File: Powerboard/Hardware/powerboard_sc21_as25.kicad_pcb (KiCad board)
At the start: 4 copper layers, 86.3 x 55.6 mm, 151 parts, among them IC1 BQ24618RGET-iclr, IC2 CP2102, J1 Thermistor Connection 103AT N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, J10 Conn_01x04_Male, J11 Conn_01x03_MountingPin, J2 Conn_01x02_Male, J3 Conn_01x02_Male, J4 Conn_01x08_Male, J5 Conn_01x04_Male, J6 Conn_01x02_Male, J7 IsolationSwitch, J8 USB_C_Receptacle_USB2.0, J9 Conn_Coaxial, Q1 RSJ250P10TL, Q10 MCH6351, Q2 RSJ250P10TL, Q3 RSJ250P10TL, Q4 RS1G120MN, Q5 RS1G120MN, Q6 MMDT2222A, Q7 RSJ250P10TL, Q8 RSJ250P10TL, Q9 MCH6351, U1 LTC4412xS6, U11 LTC4411, U2 SN65HVD230, U3 ESP32-PICO-D4, U4 SC4216H, U6 LM2679T-3.3-iclr, U7 LM2679T-3.3-iclr, U8 LTC4412xS6, U9 LTC4412xS6

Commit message: made can h and can l lines closer in length
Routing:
- net /CANL: track 38.5 -> 37.1 mm
- net GND: vias 298 -> 297
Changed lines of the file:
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@@
   (via (at 134.5 52.5) (size 0.8) (drill 0.4) (layers "F.Cu" "B.Cu") (free) (net 2))
   (via (at 126.4 63.197) (size 0.8) (drill 0.4) (layers "F.Cu" "B.Cu") (free) (net 2))
-  (via (at 95.8155 71.3) (size 0.8) (drill 0.4) (layers "F.Cu" "B.Cu") (free) (net 2))
   (via (at 117.5 78) (size 0.8) (drill 0.4) (layers "F.Cu" "B.Cu") (free) (net 2))
   (via (at 103 36.5) (size 0.8) (drill 0.4) (layers "F.Cu" "B.Cu") (free) (net 2))
@@
   (segment (start 75.745155 57.598081) (end 75.158096 57.011022) (width 0.25) (layer "B.Cu") (net 37))
   (segment (start 75.158096 57.011022) (end 75.158096 56.410831) (width 0.25) (layer "B.Cu") (net 37))
-  (segment (start 96.98952 71.84352) (end 96.98952 70.635866) (width 0.25) (layer "B.Cu") (net 39))
+  (segment (start 96.54 80.16) (end 96.54 77.958) (width 0.25) (layer "B.Cu") (net 39))
+  (segment (start 101.300449 59.749551) (end 103.355449 61.804551) (width 0.25) (layer "B.Cu") (net 39))
   (segment (start 96.54 77.958) (end 98.552 75.946) (width 0.25) (layer "B.Cu") (net 39))
-  (segment (start 98.552 75.946) (end 98.552 73.406) (width 0.25) (layer "B.Cu") (net 39))
-  (segment (start 103.29799 66.316292) (end 104.736292 66.316292) (width 0.25) (layer "B.Cu") (net 39))
-  (segment (start 96.98952 70.635866) (end 97.575386 70.05) (width 0.25) (layer "B.Cu") (net 39))
-  (segment (start 101.300449 59.749551) (end 103.355449 61.804551) (width 0.25) (layer "B.Cu") (net 39))
-  (segment (start 96.54 80.16) (end 96.54 77.958) (width 0.25) (layer "B.Cu") (net 39))
+  (segment (start 98.552 73.406) (end 96.98952 71.84352) (width 0.25) (layer "B.Cu") (net 39))
   (segment (start 104.307949 61.804551) (end 104.307949 60.062051) (width 0.25) (layer "B.Cu") (net 39))
   (segment (start 103.355449 61.804551) (end 104.307949 61.804551) (width 0.25) (layer "B.Cu") (net 39))
-  (segment (start 98.552 73.406) (end 96.98952 71.84352) (width 0.25) (layer "B.Cu") (net 39))
+  (segment (start 105.02725 61.804551) (end 104.307949 61.804551) (width 0.25) (layer "B.Cu") (net 39))
+  (segment (start 99.564282 70.05) (end 103.29799 66.316292) (width 0.25) (layer "B.Cu") (net 39))
+  (segment (start 97.575386 70.05) (end 99.564282 70.05) (width 0.25) (layer "B.Cu") (net 39))
   (segment (start 101.300449 59.749551) (end 100.710449 59.749551) (width 0.25) (layer "B.Cu") (net 39))
-  (segment (start 99.564282 70.05) (end 103.29799 66.316292) (width 0.25) (layer "B.Cu") (net 39))
   (segment (start 98.385449 60.539551) (end 99.225449 59.699551) (width 0.25) (layer "B.Cu") (net 39))
+  (segment (start 96.98952 71.84352) (end 96.98952 70.635866) (width 0.25) (layer "B.Cu") (net 39))
   (segment (start 97.431521 62.259551) (end 98.385449 61.305623) (width 0.25) (layer "B.Cu") (net 39))
-  (segment (start 105.42 61.139102) (end 104.325449 60.044551) (width 0.25) (layer "B.Cu") (net 39))
+  (segment (start 105.41 65.642584) (end 105.41 62.187301) (width 0.25) (layer "B.Cu") (net 39))
+  (segment (start 96.98952 70.635866) (end 97.575386 70.05) (width 0.25) (layer "B.Cu") (net 39))
   (segment (start 99.225449 59.699551) (end 100.660449 59.699551) (width 0.25) (layer "B.Cu") (net 39))
   (segment (start 98.385449 61.305623) (end 98.385449 60.539551) (width 0.25) (layer "B.Cu") (net 39))
-  (segment (start 97.575386 70.05) (end 99.564282 70.05) (width 0.25) (layer "B.Cu") (net 39))
-  (segment (start 105.42 65.632584) (end 105.42 61.139102) (width 0.25) (layer "B.Cu") (net 39))
-  (segment (start 104.736292 66.316292) (end 105.42 65.632584) (width 0.25) (layer "B.Cu") (net 39))
+  (segment (start 98.552 75.946) (end 98.552 73.406) (width 0.25) (layer "B.Cu") (net 39))
+  (segment (start 105.41 62.187301) (end 105.02725 61.804551) (width 0.25) (layer "B.Cu") (net 39))
+  (segment (start 103.29799 66.316292) (end 104.736292 66.316292) (width 0.25) (layer "B.Cu") (net 39))
+  (segment (start 104.736292 66.316292) (end 105.41 65.642584) (width 0.25) (layer "B.Cu") (net 39))
   (segment (start 97.389188 69.60048) (end 96.54 70.449668) (width 0.25) (layer "B.Cu") (net 40))
   (segment (start 98.354969 64.9148) (end 99.219995 65.779826) (width 0.25) (layer "B.Cu") (net 40))

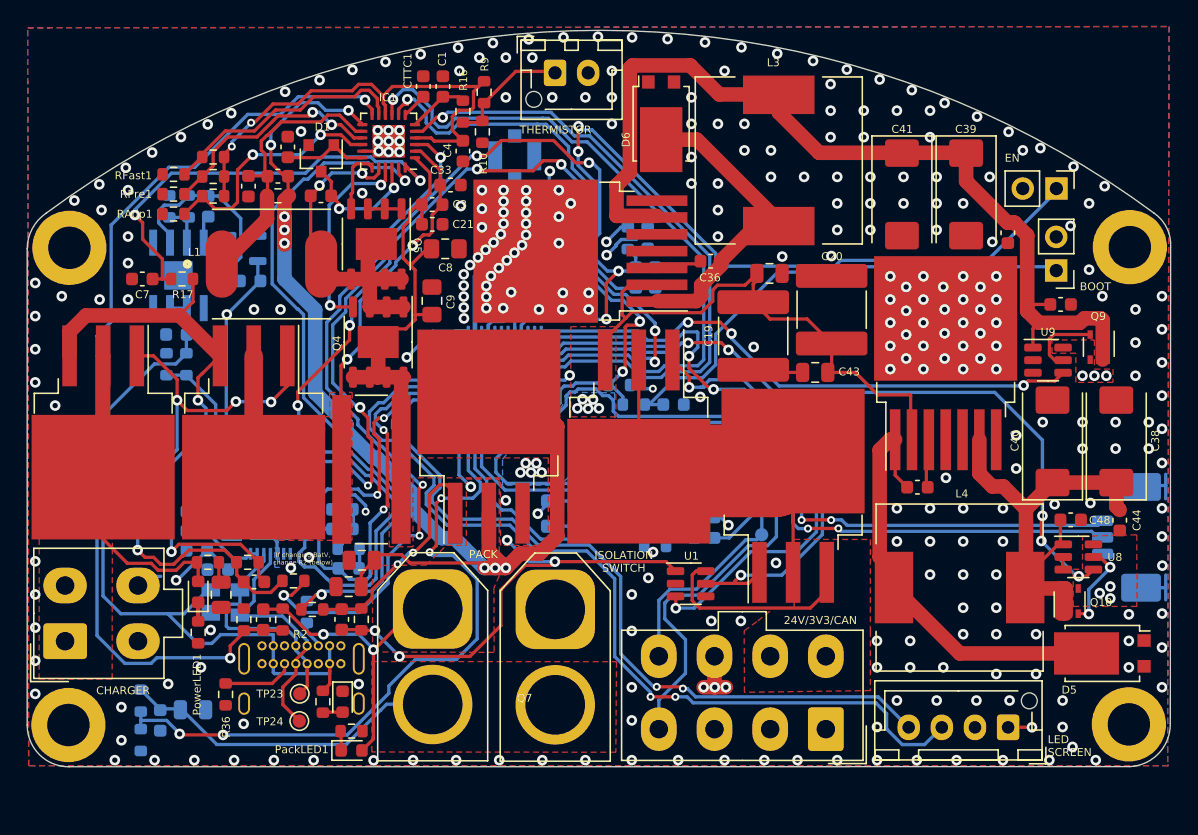
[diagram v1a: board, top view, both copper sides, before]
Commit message: re-layed out pdu to improve buck smps stability
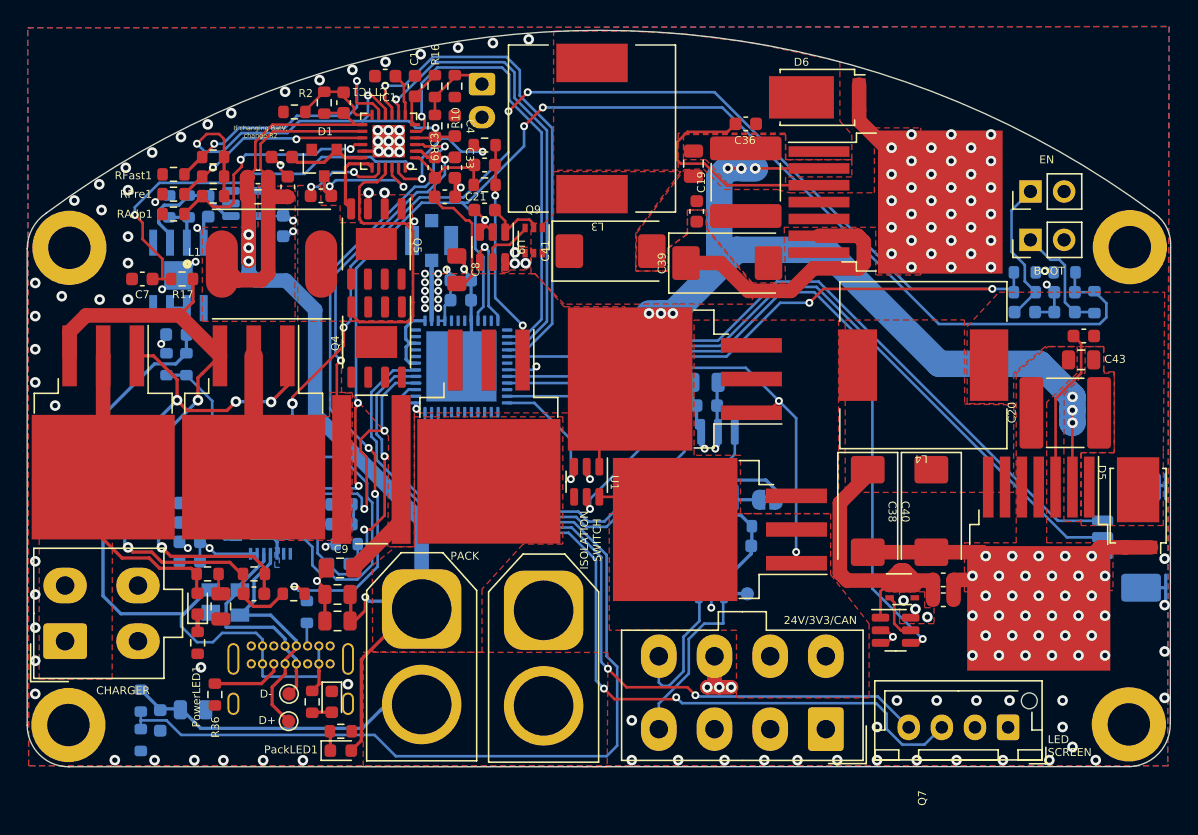
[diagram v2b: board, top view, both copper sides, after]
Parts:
- removed TP25: TestPoint, TestPoint:TestPoint_Pad_D1.0mm
- C22: footprint Capacitor_SMD:C_0805_2012Metric -> Capacitor_SMD:C_0603_1608Metric
- J1: footprint Connector_JST:JST_XH_B2B-XH-AM_1x02_P2.50mm_Vertical -> Connector_JST:JST_XH_B2B-XH-A_1x02_P2.50mm_Vertical; moved to B.Cu
- moved C49 44.0 mm to (83.4, 41.0), turned to 180 degrees
- moved Q9 43.4 mm to (87.1, 43.3)
- moved U9 42.8 mm to (84.0, 43.8), turned to -90 degrees
- moved Cff1 39.5 mm to (72.8, 32.9), turned to -90 degrees
- moved R2 39.1 mm to (71.3, 32.9), turned to -90 degrees
- moved R1 38.5 mm to (69.0, 33.6), turned to 0 degrees
- moved R32 37.4 mm to (83.4, 36.1)
- moved C15 35.9 mm to (83.4, 37.6), turned to 0 degrees
- moved R6 34.6 mm to (129.4, 48.0)
- moved R15 34.1 mm to (83.4, 39.1), turned to 180 degrees
- moved R4 33.1 mm to (127.2, 45.7), turned to 0 degrees
- moved R11 31.8 mm to (124.2, 45.7)
- moved C2 31.7 mm to (127.2, 47.2), turned to 0 degrees
- moved C17 31.0 mm to (127.2, 48.7), turned to 0 degrees
- moved R8 30.7 mm to (124.2, 47.2)
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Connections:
- Q7 pad 2: Net-(Q7-Pad2) -> Net-(J4-Pad5)
- Q7 pad 3: Net-(J4-Pad5) -> Net-(Q7-Pad3)
- Q8 pad 2: Net-(Q7-Pad2) -> +24V
- Q8 pad 3: +24V -> Net-(Q7-Pad3)
- U3 pad 13: /LPC_24V -> unconnected-(U3-Pad13)
- U3 pad 14: /3.3STAT2 -> /BATTSTAT1
- U3 pad 17: /BATTSTAT1 -> /EXT_LED
- U3 pad 20: unconnected-(U3-Pad20) -> /PDU_EN
- U3 pad 21: unconnected-(U3-Pad21) -> /3.3STAT2
- U3 pad 24: /EXT_LED -> /LPC_24V
- U3 pad 28: /PDU_EN -> unconnected-(U3-Pad28)
- U3 pad 34: /CAN_RX -> /CAN_TX
- U3 pad 35: /CAN_TX -> /CAN_RX
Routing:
- net /Battery Charger/VFB: track 72.3 -> 6.37 mm, vias 2 -> 0
- net GND: track 35.3 -> 101.2 mm, vias 297 -> 170
- net /BOOT: track 61.3 -> 118.7 mm
- net Net-(C17-Pad2): track 59.9 -> 8.63 mm, vias 2 -> 0
- net Net-(C39-Pad1): track 70.8 -> 25.2 mm
- net +3V3: track 83.7 -> 40.2 mm, vias 20 -> 17
- net Net-(IC1-Pad23): track 52.9 -> 10.2 mm
- net /LPC_24V: track 46.7 -> 9.98 mm, vias 3 -> 1
- net /3.3STAT1: track 42.8 -> 7.27 mm, vias 3 -> 1
- net /EN: track 74.3 -> 108.9 mm, vias 6 -> 4
- net /Battery Charger/Q3-D: track 108.3 -> 75.9 mm, vias 10 -> 4
- net Net-(C37-Pad2): track 31.6 -> 0.00 mm
- net Net-(Q7-Pad2): track 30.9 -> 0.00 mm
- net Net-(C18-Pad2): track 37.5 -> 11.1 mm
- net /CHARGE: track 52.6 -> 75.2 mm, vias 4 -> 0
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- added copper zone on F.Cu, net /Battery Charger/PH
- added copper zone on F.Cu, net /Battery Charger/SRP
- added copper zone on F.Cu, net Net-(C36-Pad2)
- added copper zone on F.Cu, net Net-(C37-Pad2)
- added copper zone on F.Cu, net Net-(C38-Pad1)
- added copper zone on F.Cu, net Net-(C39-Pad1)
- added copper zone on F.Cu, net Net-(Q7-Pad3)
- removed copper zone on B.Cu, net +24V
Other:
- board text added: "CAN HIGH"
- board text added: "CAN LOW"
- board text added: "D+"
- board text added: "D-"
- board text added: "If changing BatV, change R2"
- board text added: "TERM"
- board text removed: "If changing BatV, change R2 (below)"

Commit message: fixes
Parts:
- moved C22 0.52 mm to (82.1, 46.5)
- moved C24 0.52 mm to (82.1, 48.0)
- moved C8 0.50 mm to (81.3, 45.0)
- moved U3 0.25 mm to (81.9, 52.8)
- moved J4 0.24 mm to (108.9, 80.2)
- moved C40 0.22 mm to (112.1, 63.8)
- moved C38 0.22 mm to (116.9, 63.8)
- moved D5 0.20 mm to (132.9, 63.3)
- moved U7 0.20 mm to (125.0, 67.7)
- moved C44 0.14 mm to (117.9, 69.0)
- moved C48 0.14 mm to (117.9, 70.5)
- moved J7 0.10 mm to (78.7, 71.2)
- moved Q10 0.10 mm to (114.8, 69.6)
- moved U8 0.10 mm to (114.3, 72.7)
- moved C36 0.10 mm to (103.1, 34.4)
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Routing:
- net Net-(C31-Pad1): track 20.4 -> 38.8 mm
- net /SCL: track 58.7 -> 63.5 mm
- net /EN: track 108.9 -> 112.4 mm
- net /SDA: track 67.8 -> 71.0 mm
- net Net-(Q7-Pad1): track 37.0 -> 40.0 mm
- net /BOOT: track 118.7 -> 121.6 mm
- net /Battery Charger/Q1-G: track 44.3 -> 47.2 mm, vias 4 -> 2
- net Net-(IC2-Pad8): track 16.0 -> 17.6 mm
- net Net-(C38-Pad1): track 25.2 -> 24.6 mm
- net +3V3: track 40.2 -> 40.6 mm, vias 17 -> 18
- net GND: track 101.2 -> 100.8 mm, vias 170 -> 157
- removed copper zone on F.Cu, net Net-(C31-Pad1)

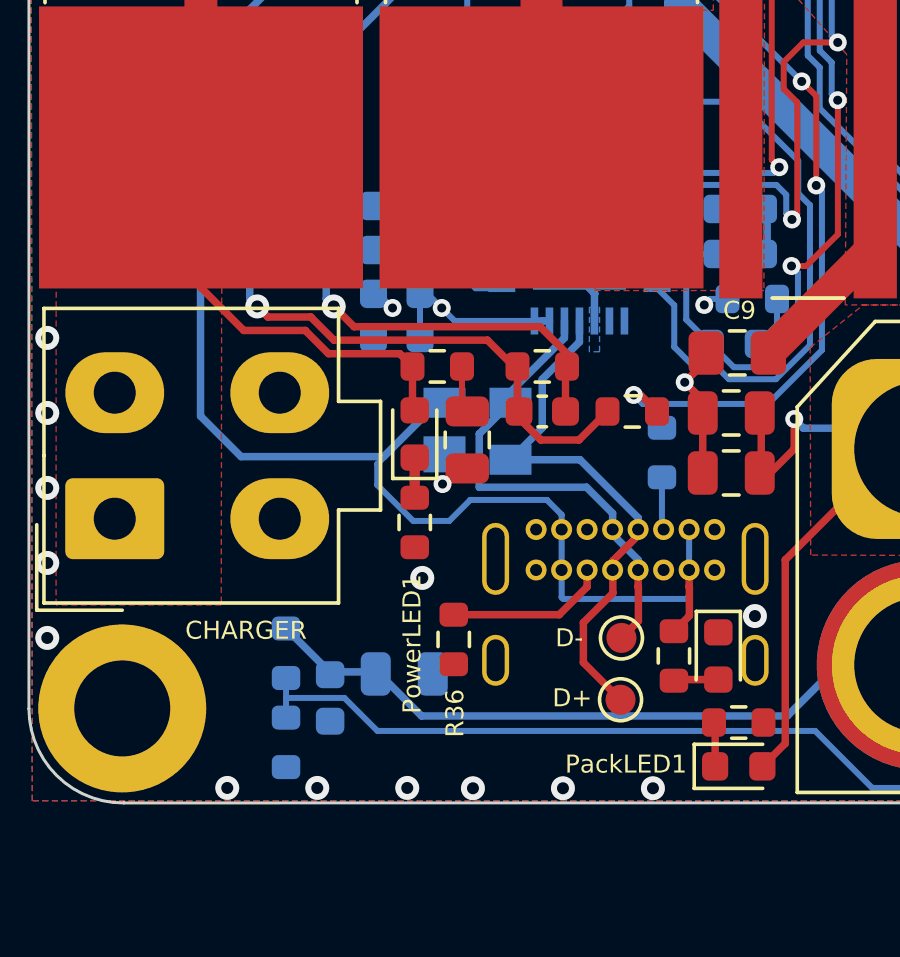
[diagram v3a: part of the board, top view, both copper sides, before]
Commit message: Added 3v3 LED, changed LED labels on silkscreen, added Kachow
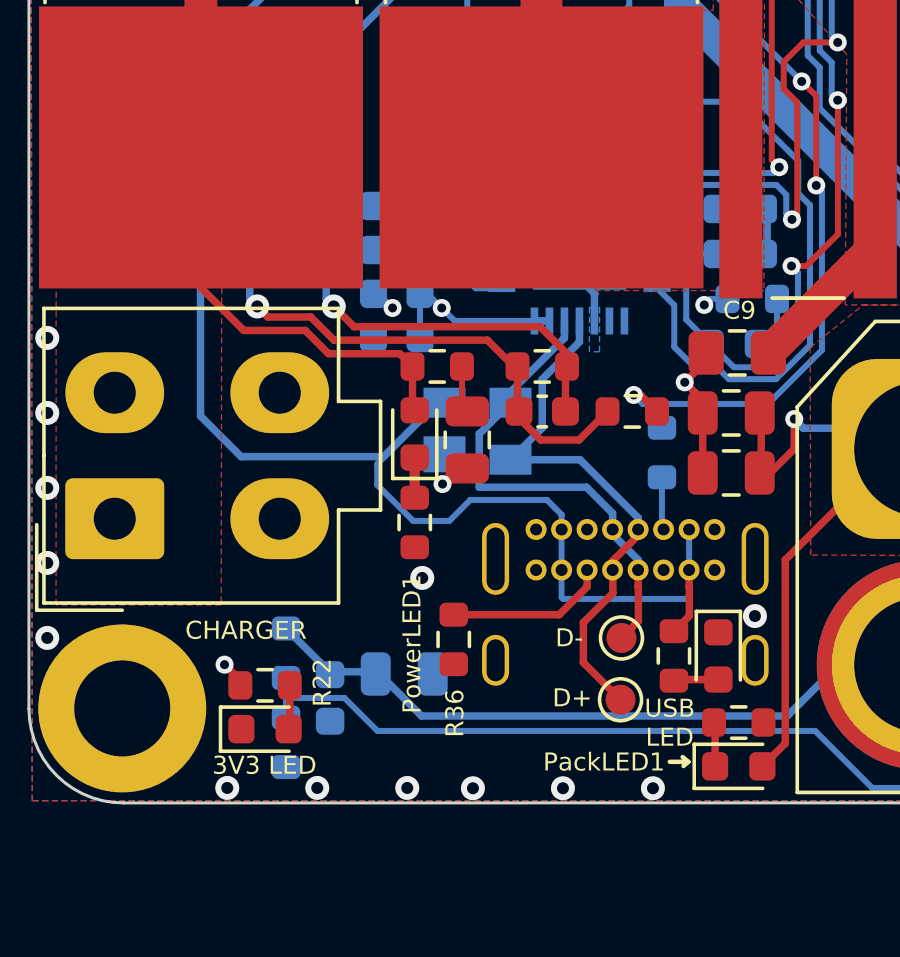
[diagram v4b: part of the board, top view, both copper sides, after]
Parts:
- added D9: LED, LED_SMD:LED_0603_1608Metric, F.Cu at (56.8, 80.5)
- added R22: 470, Resistor_SMD:R_0603_1608Metric, F.Cu at (56.8, 79.1)
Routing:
- net GND: track 100.8 -> 103.6 mm
- net Net-(D9-Pad2): track 0.00 -> 1.48 mm
- net +3V3: track 40.6 -> 41.5 mm, vias 18 -> 19
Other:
- board text added: "3V3 LED"
- board text added: "Kachow"
- board text added: "RX LED"
- board text added: "TX LED"
- board text added: "USB LED"
